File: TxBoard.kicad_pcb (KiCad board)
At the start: 2 copper layers, 94 x 31.8 mm, 21 parts, among them J1 RCA Socket, Q1 RU1J002YNTCL, SW1 Pull-Up, SW2 Input(Hi-Z)/Output, SW3 Low/High

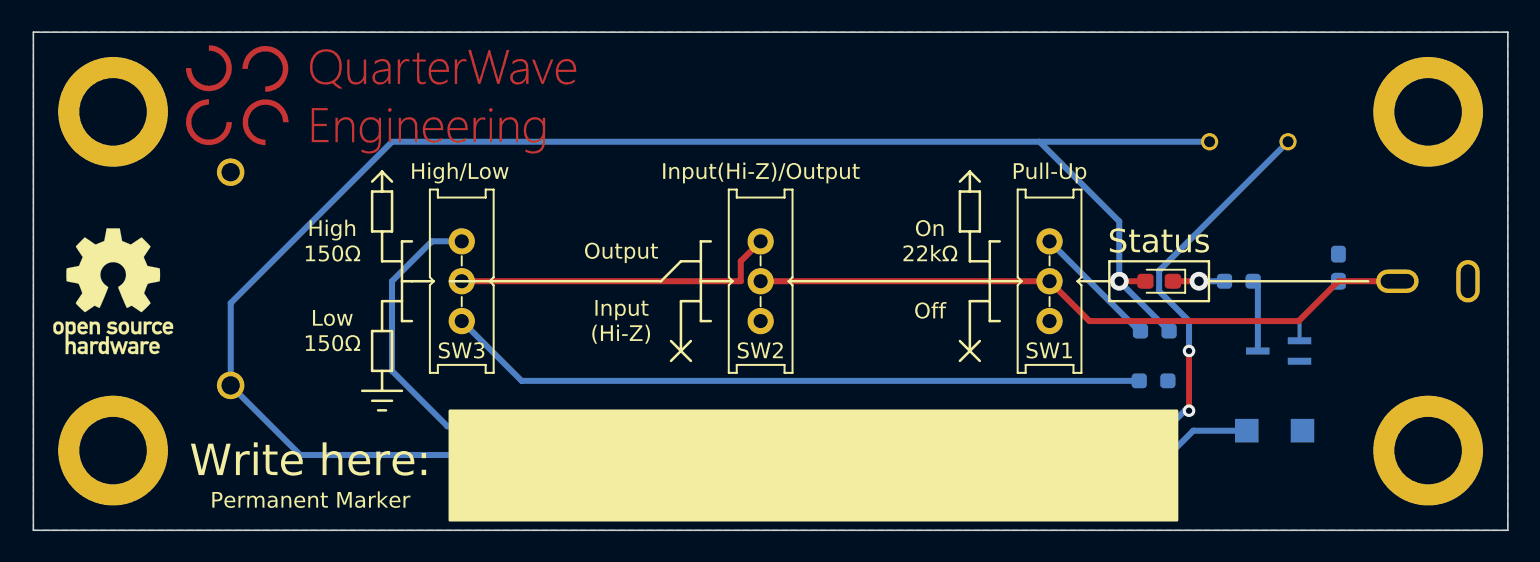
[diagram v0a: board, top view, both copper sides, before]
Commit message: PCB Rev 2
Todo: TixBoard text in mask. Logo imported too thin to clear DRC
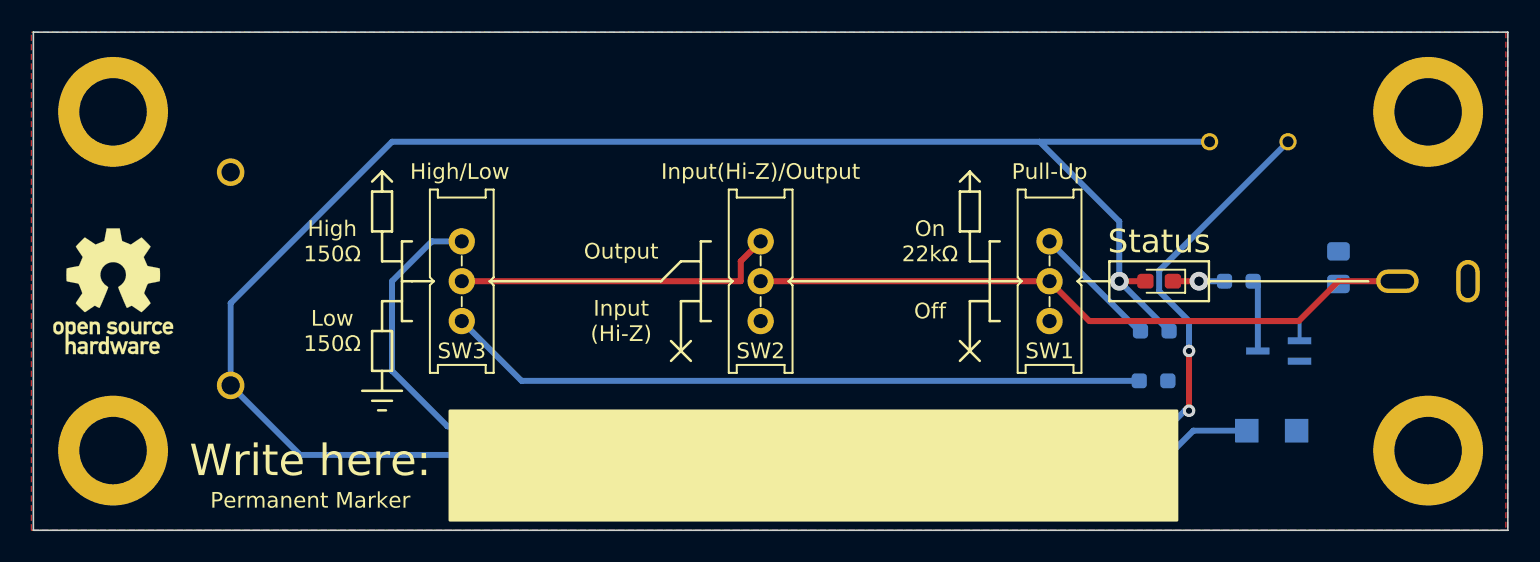
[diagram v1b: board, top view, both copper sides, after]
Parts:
- C1: footprint Capacitor_SMD:C_0603_1608Metric_Pad1.08x0.95mm_HandSolder -> Capacitor_SMD:C_0805_2012Metric_Pad1.18x1.45mm_HandSolder
- G***: footprint QuarterWave:logoWithText2 -> QuarterWave:logoWithText2Mask
- moved GND 0.38 mm to (183.5, 106.7)
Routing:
- added copper zone on F.Cu, net GND

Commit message: Prototype 1
Board final review finished, DRC issues fixed (whoever made that RCA footprint needs to learn what the polygon tool does), production files generated and will be sent out for production soon. hope it works lol
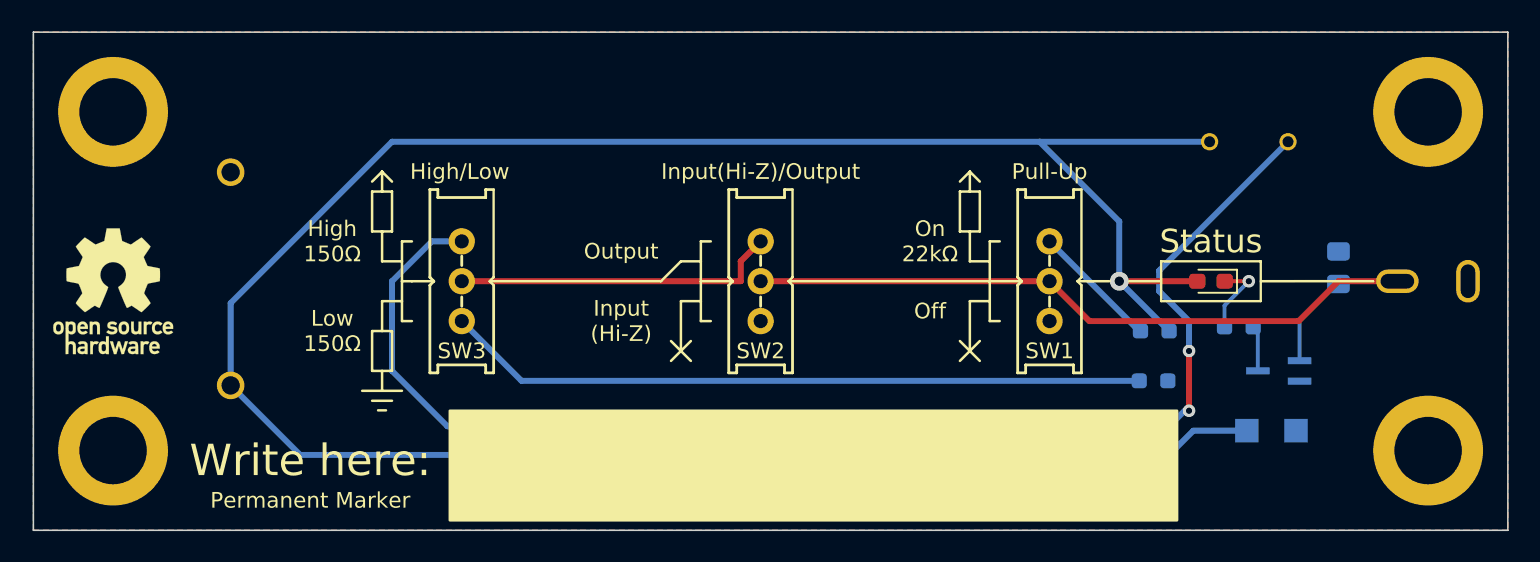
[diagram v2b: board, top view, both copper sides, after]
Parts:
- removed GND, V+: TestPoint, TestPoint:TestPoint_Pad_1.5x1.5mm
- added G***: LOGO, QuarterWave:TixBoard, F.Cu at (158.0, 85.4)
- added TP1: GND, TestPoint:TestPoint_Pad_1.5x1.5mm, B.Cu at (183.5, 106.7)
- added TP2: +V, TestPoint:TestPoint_Pad_1.5x1.5mm, B.Cu at (180.3, 106.7)
- moved D1 3.30 mm to (178.1, 97.2)
- moved R1 2.92 mm to (179.8, 100.1)
- moved Q1 1.27 mm to (182.4, 102.9)
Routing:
- net +BATT: track 156.3 -> 159.6 mm
- net Net-(D1-Pad1): track 3.29 -> 5.10 mm
- net Net-(Q1-Pad3): track 4.57 -> 2.92 mm
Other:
- board text added: "Revision 1 4/19/22"
